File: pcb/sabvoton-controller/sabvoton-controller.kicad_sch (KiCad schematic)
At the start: 33 parts, among them J1 CONTROLLER_HALL, J2 CONN_MAIN, J3 ENGINE_HALL, Q1 BSS123, U1 ESP32-WROOM-32, U2 XL7015E1, U3 XL7015E1, U4 NCP1117-3.3_SOT223, U5 LM1117-1.8, U6 BTS4140N

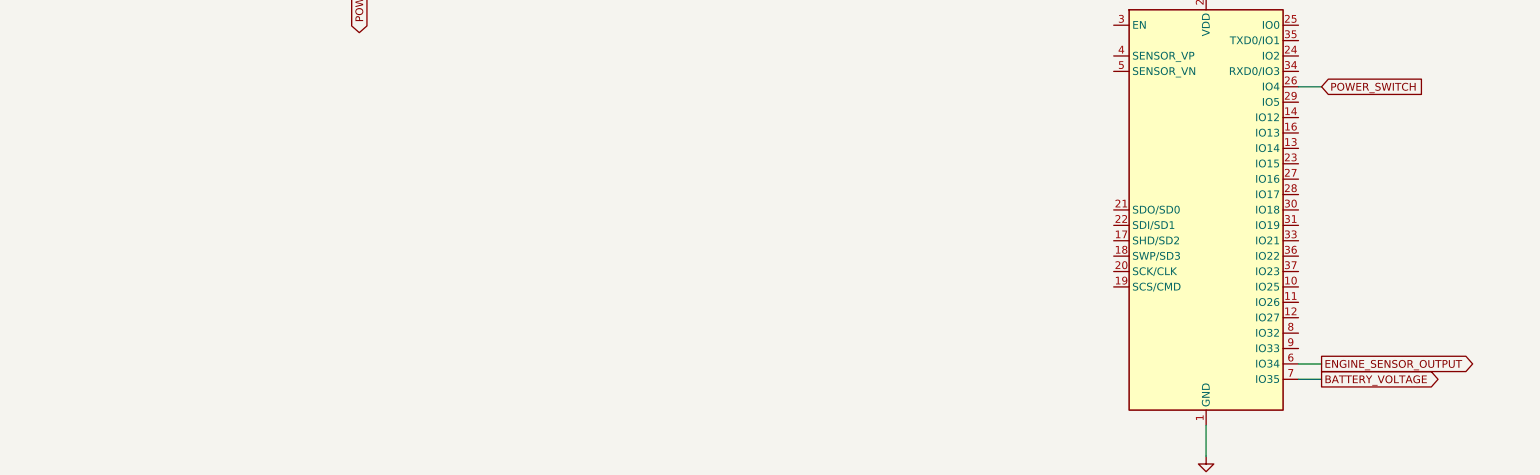
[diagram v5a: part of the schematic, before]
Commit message: Added gear switch
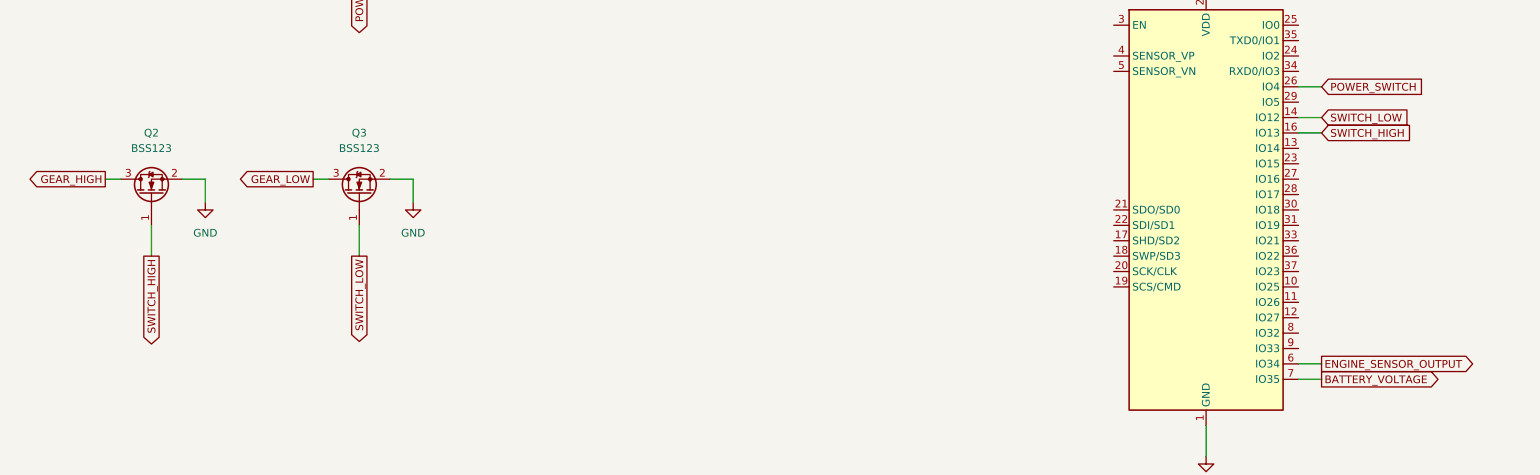
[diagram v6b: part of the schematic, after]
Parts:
- added Q2, Q3: BSS123, Package_TO_SOT_SMD:SOT-23, symbol Transistor_FET:BSS123
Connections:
- net GEAR_HIGH: now also Q2.3 (D)
- net GEAR_LOW: now also Q3.3 (D)
- net GND: now also Q2.2 (S), Q3.2 (S)
- net SWITCH_LOW: now reaches U1.14 (IO12)
- net SWITCH_LOW: now also Q3.1 (G)
- net SWITCH_HIGH: now reaches U1.16 (IO13)
- net SWITCH_HIGH: now also Q2.1 (G)
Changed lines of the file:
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@@
+    (stroke (width 0) (type default) (color 0 0 0 0))
+  )
+  (wire (pts (xy 259.08 151.13) (xy 259.08 156.21))
     (stroke (width 0) (type default) (color 0 0 0 0))
   )
@@
     (stroke (width 0) (type default) (color 0 0 0 0))
   )
+  (wire (pts (xy 217.17 143.51) (xy 219.71 143.51))
+    (stroke (width 0) (type default) (color 0 0 0 0))
+  )
   (wire (pts (xy 334.01 63.5) (xy 336.55 63.5))
     (stroke (width 0) (type default) (color 0 0 0 0))
@@
     (stroke (width 0) (type default) (color 0 0 0 0))
   )
+  (wire (pts (xy 233.68 143.51) (xy 229.87 143.51))
+    (stroke (width 0) (type default) (color 0 0 0 0))
+  )
   (wire (pts (xy 529.59 74.93) (xy 537.21 74.93))
     (stroke (width 0) (type default) (color 0 0 0 0))
   )
+  (wire (pts (xy 224.79 151.13) (xy 224.79 156.21))
+    (stroke (width 0) (type default) (color 0 0 0 0))
+  )
   (wire (pts (xy 511.81 74.93) (xy 511.81 77.47))
     (stroke (width 0) (type default) (color 0 0 0 0))
@@
     (stroke (width 0) (type default) (color 0 0 0 0))
   )
+  (wire (pts (xy 267.97 143.51) (xy 264.16 143.51))
+    (stroke (width 0) (type default) (color 0 0 0 0))
+  )
   (wire (pts (xy 508 116.84) (xy 508 114.3))
     (stroke (width 0) (type default) (color 0 0 0 0))
@@
     (stroke (width 0) (type default) (color 0 0 0 0))
   )
+  (wire (pts (xy 233.68 147.32) (xy 233.68 143.51))
+    (stroke (width 0) (type default) (color 0 0 0 0))
+  )
   (wire (pts (xy 398.78 184.15) (xy 398.78 189.23))
     (stroke (width 0) (type default) (color 0 0 0 0))
@@
     (stroke (width 0) (type default) (color 0 0 0 0))
   )
+  (wire (pts (xy 414.02 133.35) (xy 417.83 133.35))
+    (stroke (width 0) (type default) (color 0 0 0 0))
+  )
   (wire (pts (xy 412.75 59.69) (xy 412.75 66.04))
     (stroke (width 0) (type default) (color 0 0 0 0))
@@
     (stroke (width 0) (type default) (color 0 0 0 0))
   )
+  (wire (pts (xy 414.02 135.89) (xy 417.83 135.89))
+    (stroke (width 0) (type default) (color 0 0 0 0))
+  )
   (wire (pts (xy 511.81 74.93) (xy 519.43 74.93))
     (stroke (width 0) (type default) (color 0 0 0 0))
@@
     (stroke (width 0) (type default) (color 0 0 0 0))
   )
+  (wire (pts (xy 251.46 143.51) (xy 254 143.51))
+    (stroke (width 0) (type default) (color 0 0 0 0))
+  )
   (wire (pts (xy 510.54 187.96) (xy 510.54 186.69))
     (stroke (width 0) (type default) (color 0 0 0 0))
@@
     (stroke (width 0) (type default) (color 0 0 0 0))
   )
+  (wire (pts (xy 267.97 147.32) (xy 267.97 143.51))
+    (stroke (width 0) (type default) (color 0 0 0 0))
+  )
   (wire (pts (xy 410.21 59.69) (xy 410.21 66.04))
     (stroke (width 0) (type default) (color 0 0 0 0))
@@
     (effects (font (size 1.27 1.27)) (justify right))
     (property "Intersheet References" "${INTERSHEET_REFS}" (id 0) (at 339.0106 88.8336 90)
+      (effects (font (size 1.27 1.27)) (justify right) hide)
+    )
+  )
+  (global_label "GEAR_HIGH" (shape output) (at 217.17 143.51 180) (fields_autoplaced)
+    (effects (font (size 1.27 1.27)) (justify right))
+    (property "Intersheet References" "${INTERSHEET_REFS}" (id 0) (at 204.4759 143.4306 0)
       (effects (font (size 1.27 1.27)) (justify right) hide)
     )
@@
     )
   )
+  (global_label "SWITCH_HIGH" (shape input) (at 417.83 135.89 0) (fields_autoplaced)
+    (effects (font (size 1.27 1.27)) (justify left))
+    (property "Intersheet References" "${INTERSHEET_REFS}" (id 0) (at 432.5802 135.8106 0)
+      (effects (font (size 1.27 1.27)) (justify left) hide)
+    )
+  )
   (global_label "POWER_SWITCH" (shape input) (at 417.83 128.27 0) (fields_autoplaced)
     (effects (font (size 1.27 1.27)) (justify left))
@@
     )
   )
+  (global_label "SWITCH_HIGH" (shape output) (at 224.79 156.21 270) (fields_autoplaced)
+    (effects (font (size 1.27 1.27)) (justify right))
+    (property "Intersheet References" "${INTERSHEET_REFS}" (id 0) (at 224.7106 170.9602 90)
+      (effects (font (size 1.27 1.27)) (justify right) hide)
+    )
+  )
   (global_label "BATTERY_VOLTAGE" (shape input) (at 637.54 59.69 0) (fields_autoplaced)
     (effects (font (size 1.27 1.27)) (justify left))
@@
     )
   )
+  (global_label "SWITCH_LOW" (shape output) (at 259.08 156.21 270) (fields_autoplaced)
+    (effects (font (size 1.27 1.27)) (justify right))
+    (property "Intersheet References" "${INTERSHEET_REFS}" (id 0) (at 259.0006 170.2345 90)
+      (effects (font (size 1.27 1.27)) (justify right) hide)
+    )
+  )
   (global_label "B-" (shape output) (at 486.41 54.61 180) (fields_autoplaced)
     (effects (font (size 1.27 1.27)) (justify right))
@@
     )
   )
+  (global_label "GEAR_LOW" (shape output) (at 251.46 143.51 180) (fields_autoplaced)
+    (effects (font (size 1.27 1.27)) (justify right))
+    (property "Intersheet References" "${INTERSHEET_REFS}" (id 0) (at 239.4917 143.4306 0)
+      (effects (font (size 1.27 1.27)) (justify right) hide)
+    )
+  )
   (global_label "ENGINE_SENSOR" (shape output) (at 506.73 176.53 180) (fields_autoplaced)
     (effects (font (size 1.27 1.27)) (justify right))
@@
     )
   )
+  (global_label "SWITCH_LOW" (shape input) (at 417.83 133.35 0) (fields_autoplaced)
+    (effects (font (size 1.27 1.27)) (justify left))
+    (property "Intersheet References" "${INTERSHEET_REFS}" (id 0) (at 431.8545 133.2706 0)
+      (effects (font (size 1.27 1.27)) (justify left) hide)
+    )
+  )
   (symbol (lib_id "power:GND") (at 487.68 93.98 0) (unit 1)
     (in_bom yes) (on_board yes) (fields_autoplaced)
@@
     (pin "2")
   )
+  (symbol (lib_id "power:GND") (at 233.68 147.32 0) (unit 1)
+    (in_bom yes) (on_board yes) (fields_autoplaced)
+    (property "Reference" "#PWR06" (id 0) (at 233.68 153.67 0)
+      (effects (font (size 1.27 1.27)) hide)
+    )
+    (property "Value" "GND" (id 1) (at 233.68 152.4 0))
+    (property "Footprint" "" (id 2) (at 233.68 147.32 0)
+      (effects (font (size 1.27 1.27)) hide)
+    )
+    (property "Datasheet" "" (id 3) (at 233.68 147.32 0)
+      (effects (font (size 1.27 1.27)) hide)
+    )
+    (pin "1")
+  )
   (symbol (lib_id "KT_Display:XL7015E1") (at 508 83.82 180) (unit 1)
     (in_bom yes) (on_board yes) (fields_autoplaced)
@@
     (pin "1")
     (pin "2")
+  )
+  (symbol (lib_id "Transistor_FET:BSS123") (at 259.08 146.05 90) (unit 1)
+    (in_bom yes) (on_board yes) (fields_autoplaced)
+    (property "Reference" "Q3" (id 0) (at 259.08 135.89 90))
+    (property "Value" "BSS123" (id 1) (at 259.08 138.43 90))
+    (property "Footprint" "Package_TO_SOT_SMD:SOT-23" (id 2) (at 260.985 140.97 0)
+      (effects (font (size 1.27 1.27) italic) (justify left) hide)
+    )
+    (property "Datasheet" "http://www.diodes.com/assets/Datasheets/ds30366.pdf" (id 3) (at 259.08 146.05 0)
+      (effects (font (size 1.27 1.27)) (justify left) hide)
+    )
+    (pin "1")
+    (pin "2")
+    (pin "3")
+  )
+  (symbol (lib_id "Transistor_FET:BSS123") (at 224.79 146.05 90) (unit 1)
+    (in_bom yes) (on_board yes) (fields_autoplaced)
+    (property "Reference" "Q2" (id 0) (at 224.79 135.89 90))
+    (property "Value" "BSS123" (id 1) (at 224.79 138.43 90))
+    (property "Footprint" "Package_TO_SOT_SMD:SOT-23" (id 2) (at 226.695 140.97 0)
+      (effects (font (size 1.27 1.27) italic) (justify left) hide)
+    )
+    (property "Datasheet" "http://www.diodes.com/assets/Datasheets/ds30366.pdf" (id 3) (at 224.79 146.05 0)
+      (effects (font (size 1.27 1.27)) (justify left) hide)
+    )
+    (pin "1")
+    (pin "2")
+    (pin "3")
   )
   (symbol (lib_id "power:GND") (at 591.82 111.76 0) (unit 1)
@@
     (pin "5")
   )
+  (symbol (lib_id "power:GND") (at 267.97 147.32 0) (unit 1)
+    (in_bom yes) (on_board yes) (fields_autoplaced)
+    (property "Reference" "#PWR07" (id 0) (at 267.97 153.67 0)
+      (effects (font (size 1.27 1.27)) hide)
+    )
+    (property "Value" "GND" (id 1) (at 267.97 152.4 0))
+    (property "Footprint" "" (id 2) (at 267.97 147.32 0)
+      (effects (font (size 1.27 1.27)) hide)
+    )
+    (property "Datasheet" "" (id 3) (at 267.97 147.32 0)
+      (effects (font (size 1.27 1.27)) hide)
+    )
+    (pin "1")
+  )
   (symbol (lib_id "Device:C") (at 530.86 110.49 180) (unit 1)
     (in_bom yes) (on_board yes) (fields_autoplaced)
@@
       (reference "#PWR05") (unit 1) (value "GND") (footprint "")
     )
+    (path "/512bdda8-6a36-4db1-b56f-822d74895517"
+      (reference "#PWR06") (unit 1) (value "GND") (footprint "")
+    )
+    (path "/c4d17c63-5207-4b91-b42a-ad3cc36c9ecc"
+      (reference "#PWR07") (unit 1) (value "GND") (footprint "")
+    )
     (path "/503c752c-7842-4267-a639-6f3d9aa0fe2a"
       (reference "#PWR0101") (unit 1) (value "GND") (footprint "")
@@
       (reference "Q1") (unit 1) (value "BSS123") (footprint "Package_TO_SOT_SMD:SOT-23")
     )
+    (path "/95bc29b5-6381-4301-9635-467d67acbce7"
+      (reference "Q2") (unit 1) (value "BSS123") (footprint "Package_TO_SOT_SMD:SOT-23")
+    )
+    (path "/893c2100-997a-4537-ae24-d18a3ed5949a"
+      (reference "Q3") (unit 1) (value "BSS123") (footprint "Package_TO_SOT_SMD:SOT-23")
+    )
     (path "/3c54a24c-10be-4236-a15f-1623c52b157c"

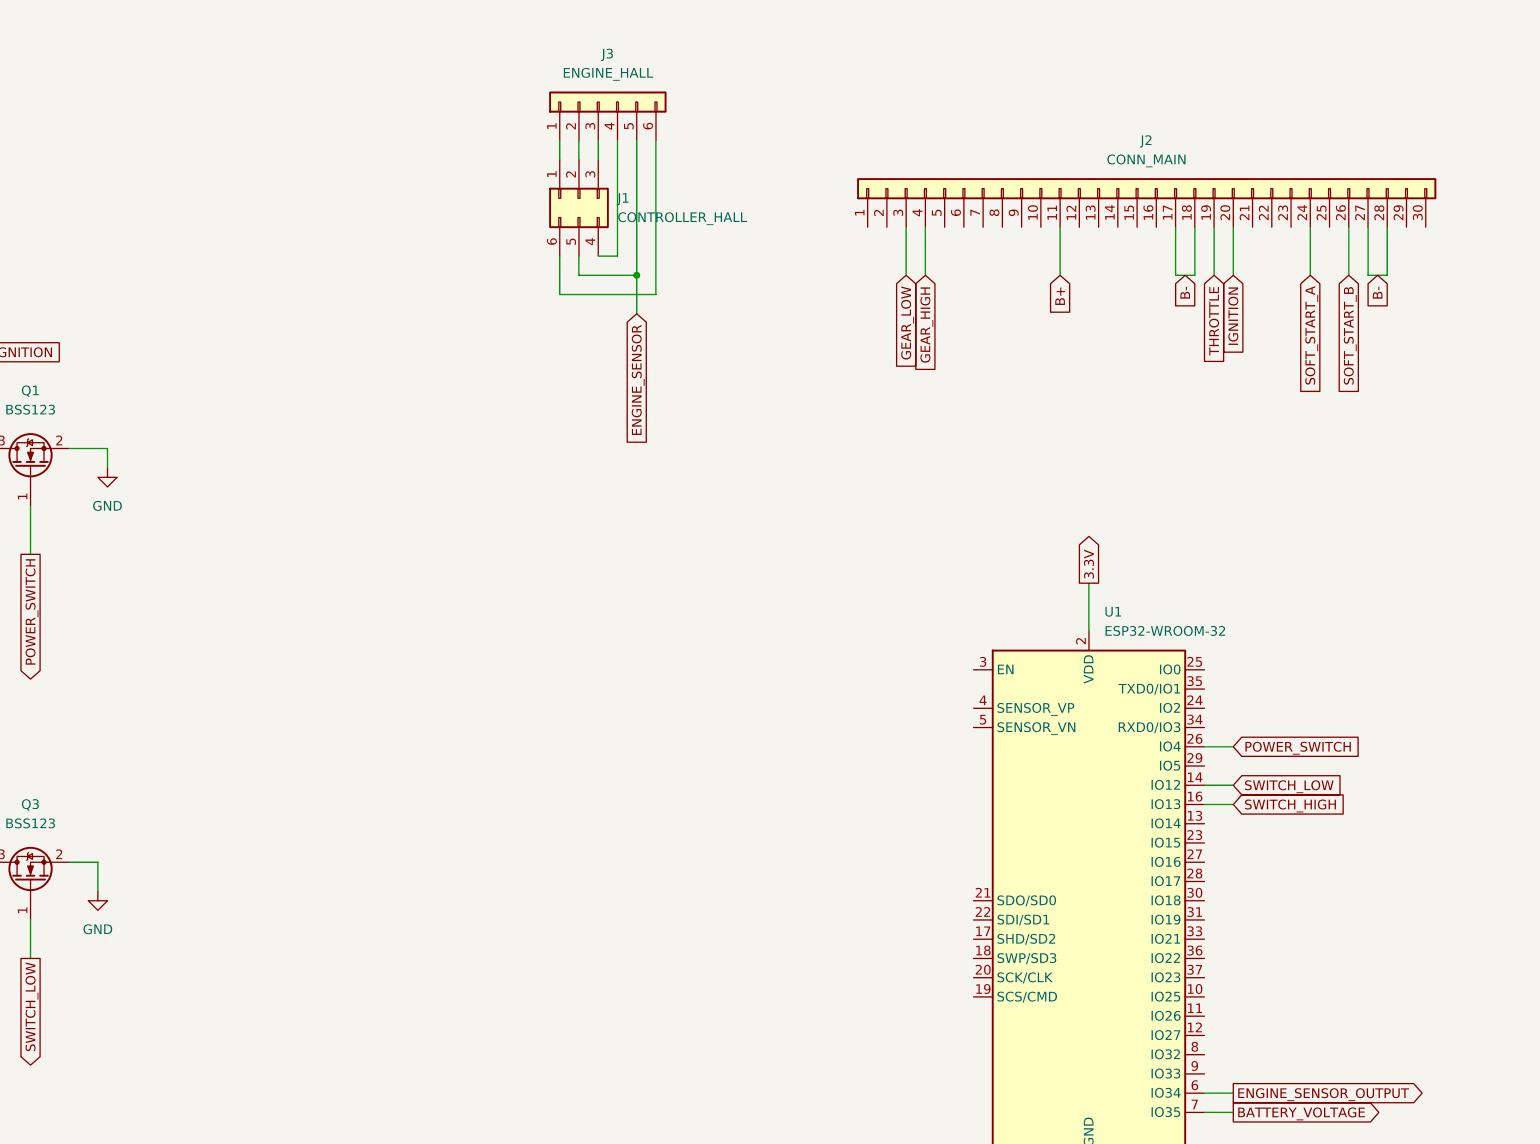
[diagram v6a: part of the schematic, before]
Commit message: Added throttle output
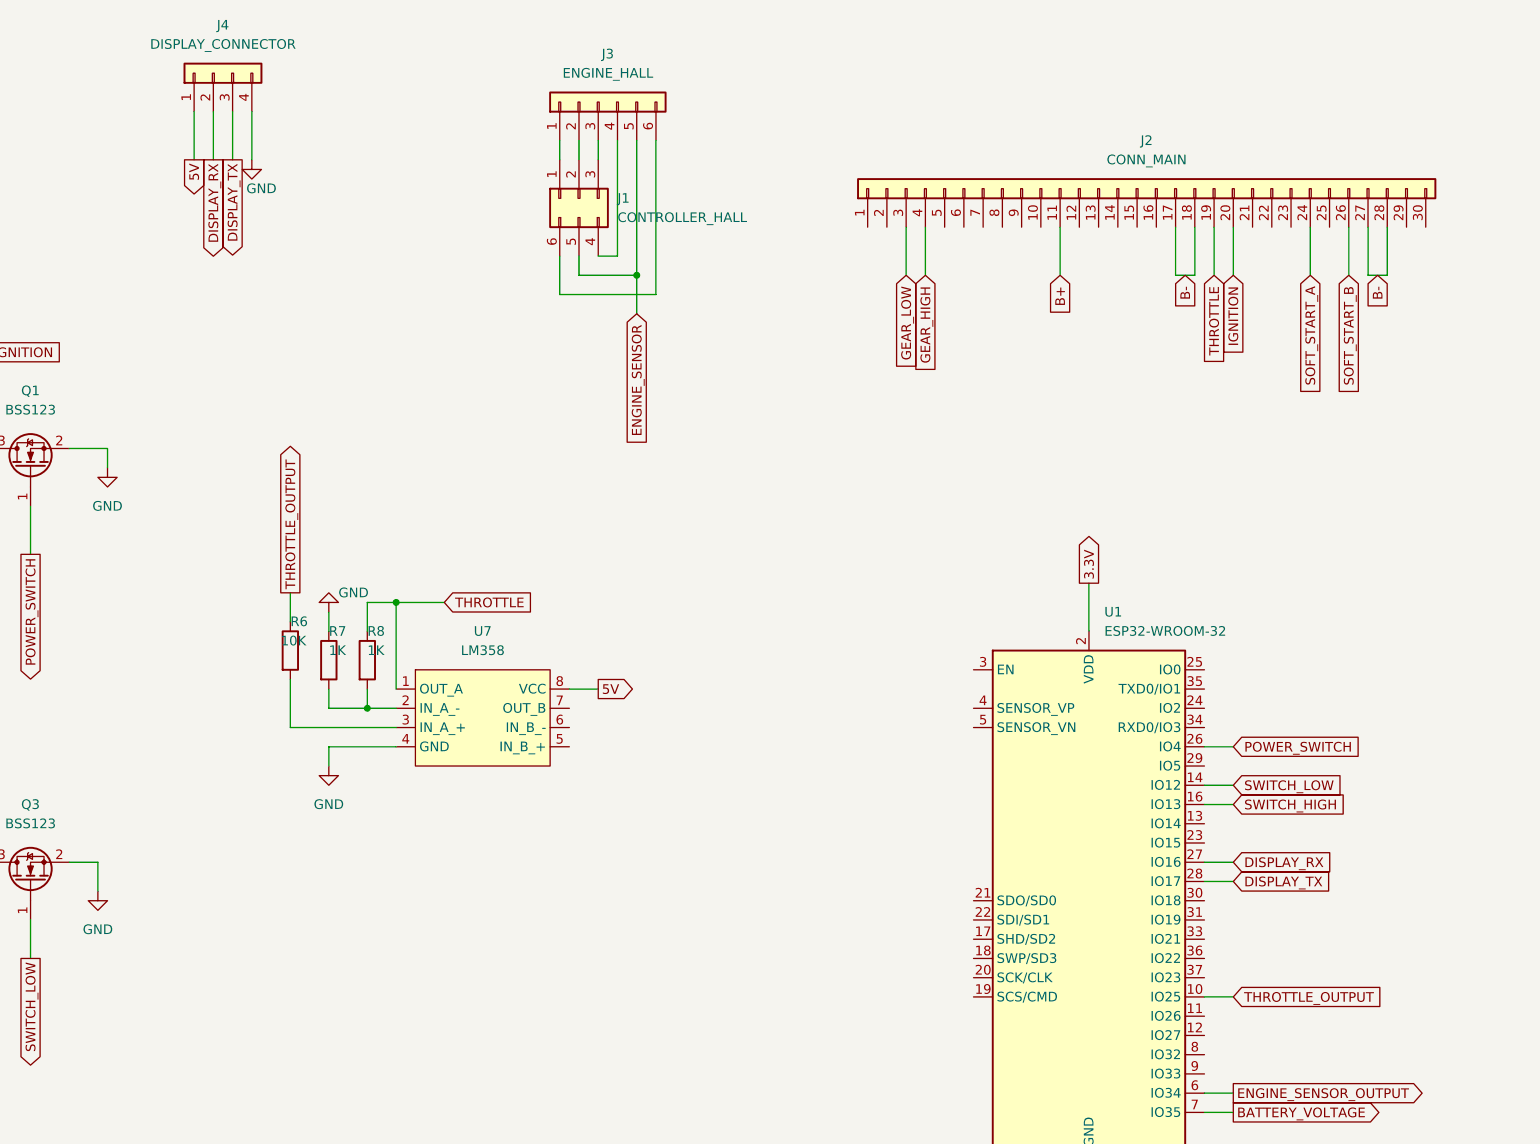
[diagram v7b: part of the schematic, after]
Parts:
- added J4: DISPLAY_CONNECTOR, symbol Connector_Generic:Conn_01x04
- added R6: 10K, symbol Device:R
- added R7, R8: 1K, symbol Device:R
- added U7: LM358, Package_SO:SO-8_5.3x6.2mm_P1.27mm, symbol KT_Display:LM358
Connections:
- net 5V: now also J4.1 (Pin_1), U7.8 (VCC)
- net GND: now also J4.4 (Pin_4), R7.1, U7.4 (GND)
- net THROTTLE: now also R8.1, U7.1 (OUT_A)
- net THROTTLE_OUTPUT: now reaches U1.10 (IO25)
- net THROTTLE_OUTPUT: now also R6.1
- net DISPLAY_RX: now reaches U1.27 (IO16)
- net DISPLAY_RX: now also J4.2 (Pin_2)
- net DISPLAY_TX: now reaches U1.28 (IO17)
- net DISPLAY_TX: now also J4.3 (Pin_3)
- new net: R7.2, R8.2, U7.2 (IN_A_-)
- new net: R6.2, U7.3 (IN_A_+)

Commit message: Added torque sensor connection
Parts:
- added J?: TORQUE_SENSOR_CONNECTOR, symbol Connector_Generic:Conn_01x04
- added R?: 10K, symbol Device:R
- added R?: 33K, symbol Device:R
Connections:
- net 12V: now also J?.1 (Pin_1)
- net GND: now also J?.4 (Pin_4), R?.1
- net PAS_SIGNAL_LOW: now reaches U1.13 (IO14)
- net PAS_SIGNAL_LOW: now also R?.2, R?.2
- net TORQUE_OUTPUT: now reaches U1.9 (IO33)
- net TORQUE_OUTPUT: now also J?.3 (Pin_3)
- new net PAS_SIGNAL: J?.2 (Pin_2), R?.1
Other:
- moved on the sheet: CFF1, CFF2, CIN1, CIN2, CIN3, CIN4, CIN5, CIN6, COUT1, COUT2, COUT3, COUT4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
